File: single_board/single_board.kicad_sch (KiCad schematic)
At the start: 128 parts, among them J1 PB_Vertical, J10 PB_Vertical, J11 PB_Vertical, J12 2.54, J13 PB_Vertical, J14 PB_Vertical, J15 PB_Vertical, J16 PB_Vertical, J17 JST-GH, J18 PB_Vertical, J19 PB_Vertical, J2 SWD, J20 PB_Vertical, J21 PB_Vertical, J22 PB_Vertical, J23 SPI Debug, J24 BOOTSEL, J25 JST-GH, J26 JST_GH, J27 JST_GH, J28 JST_GH, J29 PB_Vertical, J3 Power, J30 JST_GH, J31 JST_GH, J4 USB_C_Receptacle_USB2.0_16P, J5 JST_GH, J6 PB_Vertical, J7 PB_Vertical, J8 PB_Vertical, J9 PB_Vertical, Q2 AO3400A, SW1 Button, SW2 Button, SW3 Button, U1 AP2112K-3.3, U2 USBLC6-2SC6, U3 TJA1042, U4 LSM6DSVTR, U5 STM32G474VBT6, Y1 ABM8-16MHz

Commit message: Minor changes
going through bom
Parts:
- removed Q2: AO3400A, Package_TO_SOT_SMD:SOT-23, symbol Transistor_FET:AO3400A
- removed R33: 100, Resistor_SMD:R_0402_1005Metric, symbol Device:R_Small
- removed R34: 10k, Resistor_SMD:R_0402_1005Metric, symbol Device:R_Small
- added Q1: MMBT3904LT1G, Package_TO_SOT_SMD:SOT-23, symbol Transistor_BJT:Q_NPN_BEC
- added R35: 1k, Resistor_SMD:R_0402_1005Metric, symbol Device:R_Small
- renumbered D11 to D10, D12 to D11, D4 to D3, D5 to D4, D6 to D5, D7 to D6, D8 to D7, D9 to D8, D10 to D9, R12 to R10, R13 to R11, R14 to R12, R15 to R13, R16 to R14, R17 to R15, R18 to R16, R19 to R17, R20 to R18, R21 to R19, R22 to R20, R23 to R21, R36 to R22, R24 to R23, R35 to R24, R4 to R3, R38 to R31, R37 to R32, R31 to R33, R32 to R34, R5 to R4, R7 to R5, R8 to R6, R9 to R7, R10 to R8, R11 to R9
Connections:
- net GND: now also Q1.2 (E)
- net LASER_SIG: now also R35.1
- net at J30.1 (Pin_1): now also Q1.3 (C)
- new net: Q1.1 (B), R35.2
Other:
- note added: "Low side npn"
- note removed: "Low side N-MOS"
- moved on the sheet: C32, J27, J30, R26

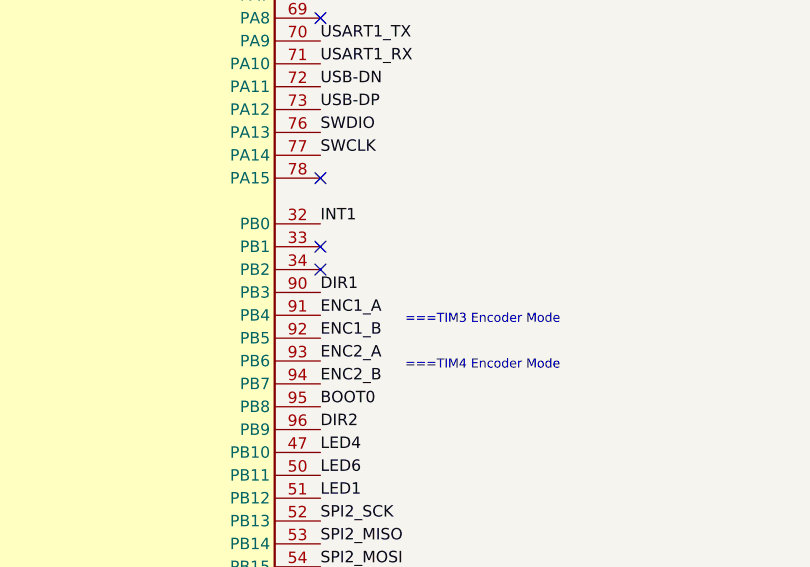
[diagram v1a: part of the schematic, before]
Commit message: Label SWO
Label SWO in schematic
Label SWO in pcb editor, user comments
PB3
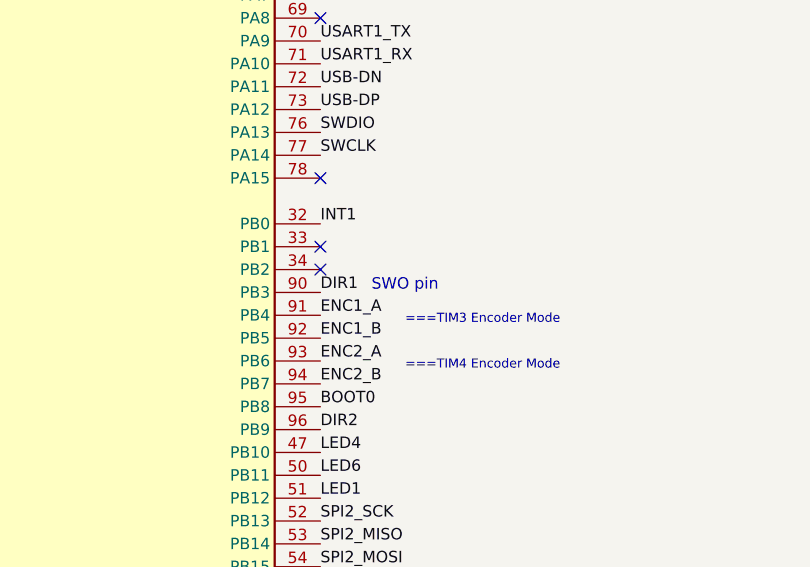
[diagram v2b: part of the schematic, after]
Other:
- note added: "SWO pin"
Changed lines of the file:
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@@
+		)
+	)
+	(text "SWO pin"
+		(exclude_from_sim no)
+		(at 311.658 253.238 0)
+		(effects
+			(font
+				(size 1.27 1.27)
+			)
 		)
 	)

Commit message: Specify IMU
LSM6DSRXTR
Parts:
- U4: value LSM6DSVTR -> LSM6DSRXTR
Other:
- note added: "SPI 4-wire"
- note removed: "Mode 0 SPI 4-wire"
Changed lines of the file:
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@@
 		)
 	)
-	(text "Mode 0\nSPI 4-wire"
+	(text "SPI 4-wire"
 		(exclude_from_sim no)
 		(at 487.68 207.264 0)
@@
 			)
 		)
-		(property "Value" "LSM6DSVTR"
+		(property "Value" "LSM6DSRXTR"
 			(at 504.19 234.95 0)
 			(show_name no)
